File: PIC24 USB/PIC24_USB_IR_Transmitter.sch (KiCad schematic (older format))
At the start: 24 parts, among them CON1 USB-MINI-B, P1 CONN_6, P2 CONN_4, P3 CONN_6, P4 CONN_6, P5 CONN_4, P6 CONN_1, P7 CONN_8, P8 CONN_8X2, Q1 2N7002, U2 LM1117_SOT223_3V3

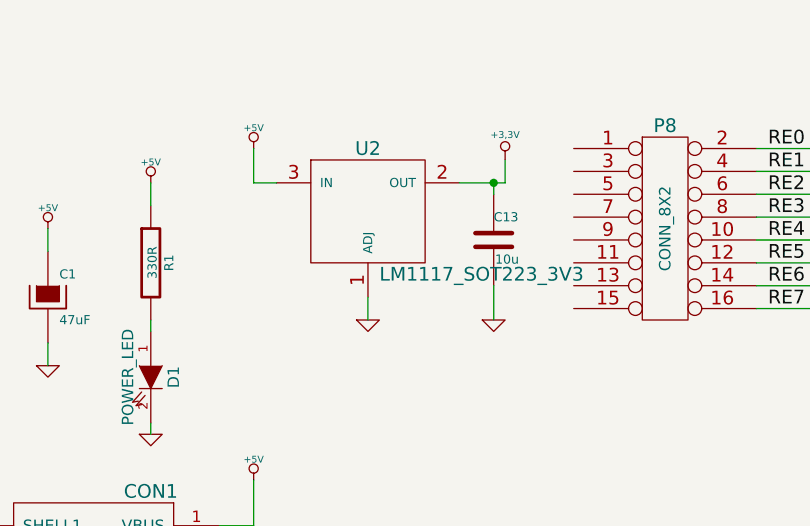
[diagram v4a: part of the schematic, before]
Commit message: converted kicad project for newer version from kicad.nosoftware.cz
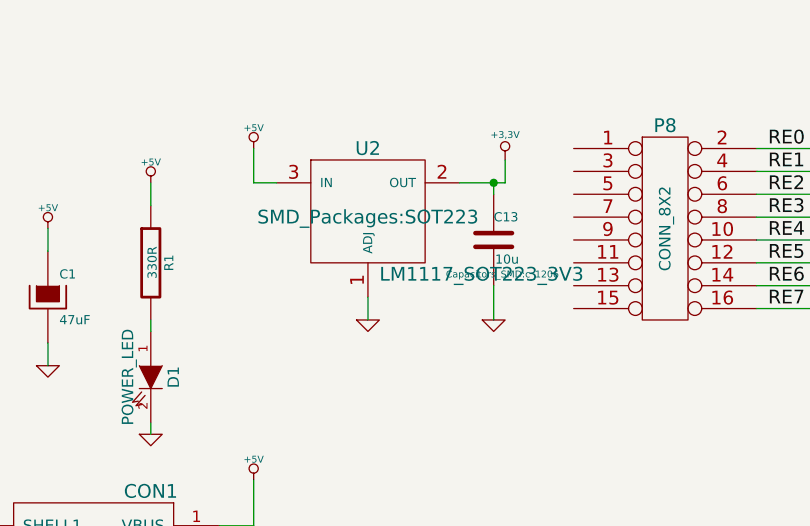
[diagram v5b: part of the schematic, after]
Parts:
- C1: footprint (none) -> c_tant_B
- C13: footprint ~ -> Capacitors_SMD:c_1206
- C2, C5, C6: footprint (none) -> Capacitors_SMD:c_0603
- CON1: footprint (none) -> Connect:USB_MINI_B
- D1, D2: footprint (none) -> LEDs:LED-0603
- D3: footprint (none) -> LEDs:LED-3MM
- P1: footprint (none) -> Connect:PINHEAD1-6
- P2, P5: footprint (none) -> Pin_Headers:Pin_Header_Straight_1x04
- P3, P4: footprint (none) -> Pin_Headers:Pin_Header_Straight_1x06
- P6: footprint (none) -> Pin_Headers:Pin_Header_Straight_1x01
- P7: footprint (none) -> pin_array_8_50mil
- P8: footprint (none) -> Pin_Headers:Pin_Header_Straight_2x08
- Q1: footprint (none) -> Transistors_SMD:sot23
- R1, R3, R5, R6: footprint (none) -> SMD_Packages:SM0603_Resistor
- R4: footprint (none) -> SMD_Packages:SM1206
- U2: footprint ~ -> SMD_Packages:SOT223
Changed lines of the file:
@@
-EESchema Schematic File Version 2  date 03.08.2014 21:39:24
+EESchema Schematic File Version 2
 LIBS:power
 LIBS:device
@@
 LIBS:microchip_hele
 LIBS:PIC24_USB_IR_Transmitter-cache
-EELAYER 27 0
+EELAYER 24 0
 EELAYER END
 $Descr A4 11693 8268
@@
 F 0 "CON1" H 1200 3600 60  0000 C CNN
 F 1 "USB-MINI-B" H 1400 2650 60  0000 C CNN
-F 2 "" H 1450 3150 60  0000 C CNN
+F 2 "Connect:USB_MINI_B" H 1450 3150 60  0001 C CNN
 F 3 "" H 1450 3150 60  0000 C CNN
 	1    1450 3150
@@
 F 0 "C1" H 1300 1950 40  0000 L CNN
 F 1 "47uF" H 1300 1750 40  0000 L CNN
-F 2 "" H 1350 1700 30  0000 C CNN
+F 2 "c_tant_B" H 1350 1700 30  0001 C CNN
 F 3 "" H 1250 1850 300 0000 C CNN
 	1    1250 1850
@@
 F 0 "C2" H 4950 4450 40  0000 L CNN
 F 1 "100n" H 4956 4265 40  0000 L CNN
-F 2 "" H 4988 4200 30  0000 C CNN
+F 2 "Capacitors_SMD:c_0603" H 4988 4200 30  0001 C CNN
 F 3 "" H 4950 4350 60  0000 C CNN
 	1    4950 4350
@@
 F 0 "C6" H 9750 5450 40  0000 L CNN
 F 1 "100n" H 9756 5265 40  0000 L CNN
-F 2 "" H 9788 5200 30  0000 C CNN
+F 2 "Capacitors_SMD:c_0603" H 9788 5200 30  0001 C CNN
 F 3 "" H 9750 5350 60  0000 C CNN
 	1    9750 5350
@@
 F 0 "C5" H 9600 4850 40  0000 L CNN
 F 1 "100n" H 9606 4665 40  0000 L CNN
-F 2 "" H 9638 4600 30  0000 C CNN
+F 2 "Capacitors_SMD:c_0603" H 9638 4600 30  0001 C CNN
 F 3 "" H 9600 4750 60  0000 C CNN
 	1    9600 4750
@@
 F 0 "Q1" H 8960 2170 60  0000 R CNN
 F 1 "2N7002" H 8960 1850 60  0000 R CNN
-F 2 "" H 8950 2000 60  0000 C CNN
+F 2 "Transistors_SMD:sot23" H 8950 2000 60  0001 C CNN
 F 3 "" H 8950 2000 60  0000 C CNN
 	1    8950 2000
@@
 F 0 "R4" V 9130 1050 40  0000 C CNN
 F 1 "100R" V 9057 1051 40  0000 C CNN
-F 2 "" V 8980 1050 30  0000 C CNN
+F 2 "SMD_Packages:SM1206" V 8980 1050 30  0001 C CNN
 F 3 "" H 9050 1050 30  0000 C CNN
 	1    9050 1050
@@
 F 0 "D3" H 9050 1650 50  0000 C CNN
 F 1 "IR_LED" H 9050 1450 50  0000 C CNN
-F 2 "" H 9050 1550 60  0000 C CNN
+F 2 "LEDs:LED-3MM" H 9050 1550 60  0001 C CNN
 F 3 "" H 9050 1550 60  0000 C CNN
 	1    9050 1550
@@
 F 0 "P3" V 3800 3600 60  0000 C CNN
 F 1 "CONN_6" V 3900 3600 60  0000 C CNN
-F 2 "" H 3850 3600 60  0000 C CNN
+F 2 "Pin_Headers:Pin_Header_Straight_1x06" H 3850 3600 60  0001 C CNN
 F 3 "" H 3850 3600 60  0000 C CNN
 	1    3850 3600
@@
 F 0 "R3" V 4530 5450 40  0000 C CNN
 F 1 "330R" V 4457 5451 40  0000 C CNN
-F 2 "" V 4380 5450 30  0000 C CNN
+F 2 "SMD_Packages:SM0603_Resistor" V 4380 5450 30  0001 C CNN
 F 3 "" H 4450 5450 30  0000 C CNN
 	1    4450 5450
@@
 F 0 "D2" H 4450 6050 50  0000 C CNN
 F 1 "USER_LED" H 4450 5850 50  0000 C CNN
-F 2 "" H 4450 5950 60  0000 C CNN
+F 2 "LEDs:LED-0603" H 4450 5950 60  0001 C CNN
 F 3 "" H 4450 5950 60  0000 C CNN
 	1    4450 5950
@@
 F 0 "R1" V 1780 1700 40  0000 C CNN
 F 1 "330R" V 1707 1701 40  0000 C CNN
-F 2 "" V 1630 1700 30  0000 C CNN
+F 2 "SMD_Packages:SM0603_Resistor" V 1630 1700 30  0001 C CNN
 F 3 "" H 1700 1700 30  0000 C CNN
 	1    1700 1700
@@
 F 0 "D1" H 1700 2300 50  0000 C CNN
 F 1 "POWER_LED" H 1700 2100 50  0000 C CNN
-F 2 "" H 1700 2200 60  0000 C CNN
+F 2 "LEDs:LED-0603" H 1700 2200 60  0001 C CNN
 F 3 "" H 1700 2200 60  0000 C CNN
 	1    1700 2200
@@
 F 0 "P4" V 4600 6700 60  0000 C CNN
 F 1 "CONN_6" V 4700 6700 60  0000 C CNN
-F 2 "" H 4650 6700 60  0000 C CNN
+F 2 "Pin_Headers:Pin_Header_Straight_1x06" H 4650 6700 60  0001 C CNN
 F 3 "" H 4650 6700 60  0000 C CNN
 	1    4650 6700
@@
 F 0 "P5" V 8750 3250 50  0000 C CNN
 F 1 "CONN_4" V 8850 3250 50  0000 C CNN
-F 2 "" H 8800 3250 60  0000 C CNN
+F 2 "Pin_Headers:Pin_Header_Straight_1x04" H 8800 3250 60  0001 C CNN
 F 3 "" H 8800 3250 60  0000 C CNN
 	1    8800 3250
@@
 F 0 "P2" V 3200 4850 50  0000 C CNN
 F 1 "CONN_4" V 3300 4850 50  0000 C CNN
-F 2 "" H 3250 4850 60  0000 C CNN
+F 2 "Pin_Headers:Pin_Header_Straight_1x04" H 3250 4850 60  0001 C CNN
 F 3 "" H 3250 4850 60  0000 C CNN
 	1    3250 4850
@@
 F 0 "P1" V 1400 5700 60  0000 C CNN
 F 1 "CONN_6" V 1500 5700 60  0000 C CNN
-F 2 "" H 1450 5700 60  0000 C CNN
+F 2 "Connect:PINHEAD1-6" H 1450 5700 60  0001 C CNN
 F 3 "" H 1450 5700 60  0000 C CNN
 	1    1450 5700
@@
 F 0 "R5" V 3880 4500 40  0000 C CNN
 F 1 "4k7" V 3807 4501 40  0000 C CNN
-F 2 "" V 3730 4500 30  0000 C CNN
+F 2 "SMD_Packages:SM0603_Resistor" V 3730 4500 30  0001 C CNN
 F 3 "" H 3800 4500 30  0000 C CNN
 	1    3800 4500
@@
 F 0 "R6" V 4030 4500 40  0000 C CNN
 F 1 "4k7" V 3957 4501 40  0000 C CNN
-F 2 "" V 3880 4500 30  0000 C CNN
+F 2 "SMD_Packages:SM0603_Resistor" V 3880 4500 30  0001 C CNN
 F 3 "" H 3950 4500 30  0000 C CNN
 	1    3950 4500
@@
 F 0 "P6" H 9680 4350 40  0000 L CNN
 F 1 "CONN_1" H 9600 4405 30  0001 C CNN
-F 2 "" H 9600 4350 60  0000 C CNN
+F 2 "Pin_Headers:Pin_Header_Straight_1x01" H 9600 4350 60  0001 C CNN
 F 3 "" H 9600 4350 60  0000 C CNN
 	1    9600 4350
@@
 F 0 "P7" V 1400 6850 60  0000 C CNN
 F 1 "CONN_8" V 1500 6850 60  0000 C CNN
-F 2 "" H 1450 6850 60  0000 C CNN
+F 2 "pin_array_8_50mil" H 1450 6850 60  0001 C CNN
 F 3 "" H 1450 6850 60  0000 C CNN
 	1    1450 6850
@@
 F 0 "U2" H 2650 1800 60  0000 C CNN
 F 1 "LM1117_SOT223_3V3" H 2700 1250 60  0000 L CNN
-F 2 "~" H 2650 1500 60  0000 C CNN
+F 2 "SMD_Packages:SOT223" H 2650 1500 60  0000 C CNN
 F 3 "~" H 2650 1500 60  0000 C CNN
 	1    2650 1500
@@
 F 0 "C13" H 3200 1700 40  0000 L CNN
 F 1 "10u" H 3206 1515 40  0000 L CNN
-F 2 "~" H 3238 1450 30  0000 C CNN
+F 2 "Capacitors_SMD:c_1206" H 3238 1450 30  0000 C CNN
 F 3 "~" H 3200 1600 60  0000 C CNN
 	1    3200 1600
@@
 F 0 "P8" H 3950 2000 60  0000 C CNN
 F 1 "CONN_8X2" V 3950 1550 50  0000 C CNN
-F 2 "" H 3950 1550 60  0000 C CNN
+F 2 "Pin_Headers:Pin_Header_Straight_2x08" H 3950 1550 60  0001 C CNN
 F 3 "" H 3950 1550 60  0000 C CNN
 	1    3950 1550
